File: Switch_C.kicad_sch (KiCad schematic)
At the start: 4 parts, among them U1601 TMCS1101A2UQDT

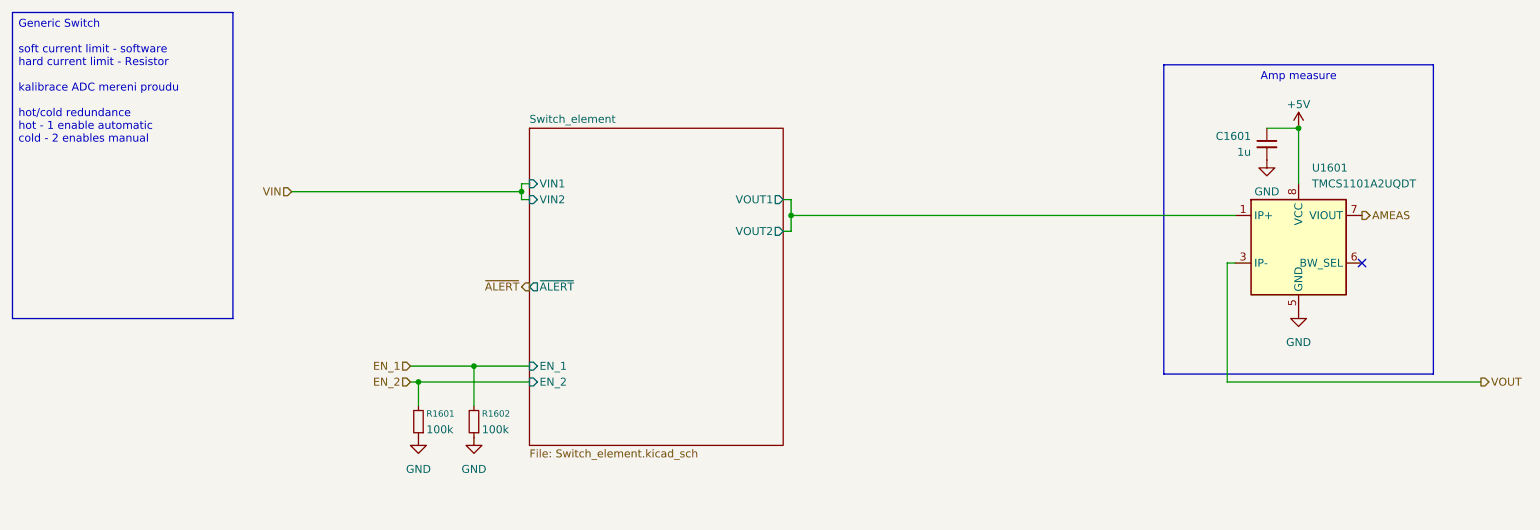
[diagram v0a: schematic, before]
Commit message: updated battery pack module; updated solar inputs module
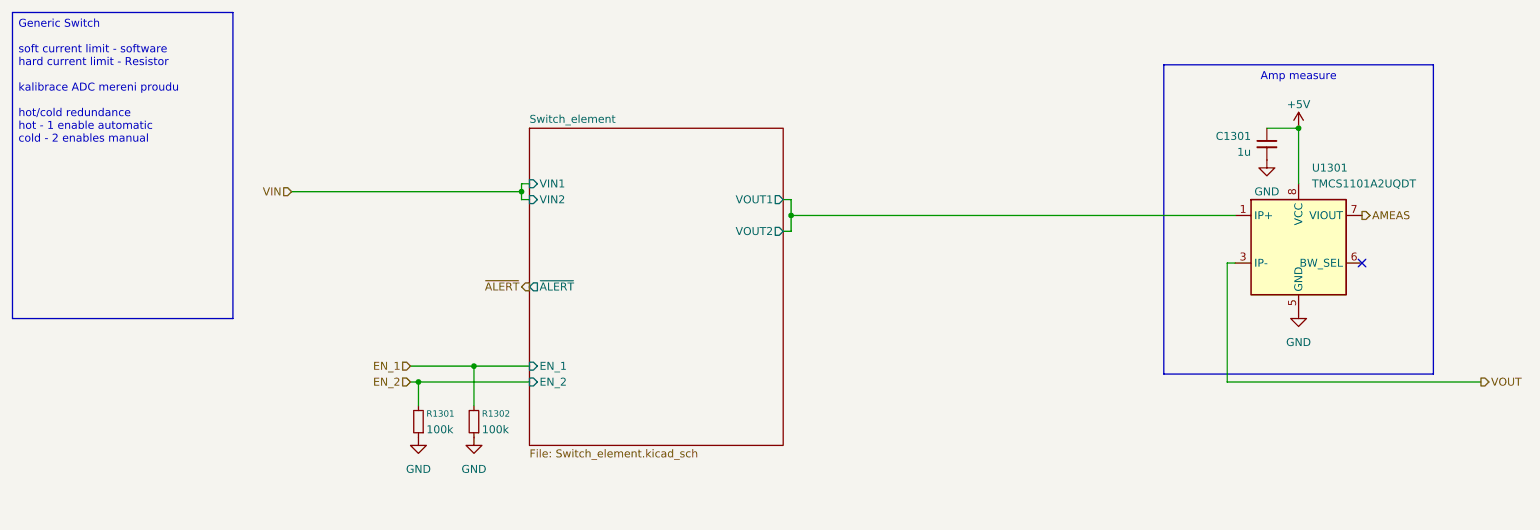
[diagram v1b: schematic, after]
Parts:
- renumbered C1601 to C1301, R1601 to R1301, R1602 to R1302, U1601 to U1301

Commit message: added values to most parts
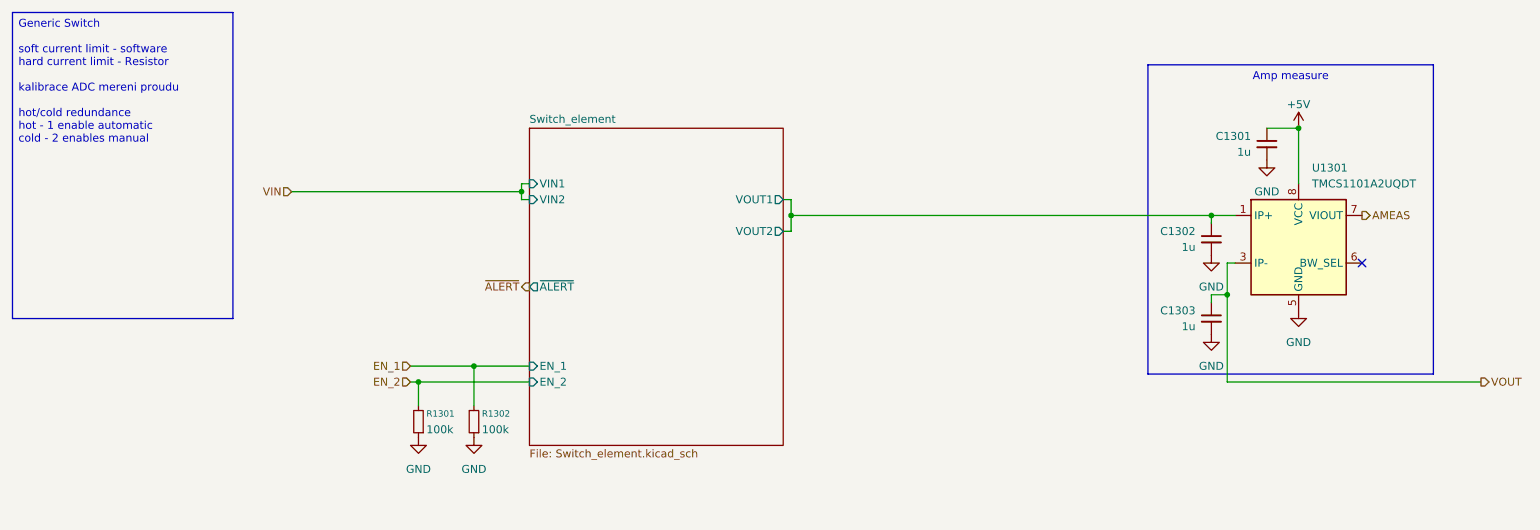
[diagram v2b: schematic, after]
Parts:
- added C1302, C1303: 1u, Capacitor_SMD:C_0603_1608Metric_Pad1.08x0.95mm_HandSolder, symbol Device:C_Small
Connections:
- net GND: now also C1302.2, C1303.2
- net Switch_element/VOUT1: now also C1302.1
- net VOUT: now also C1303.1

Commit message: deleted unused sheets, added standalone current measure sheet
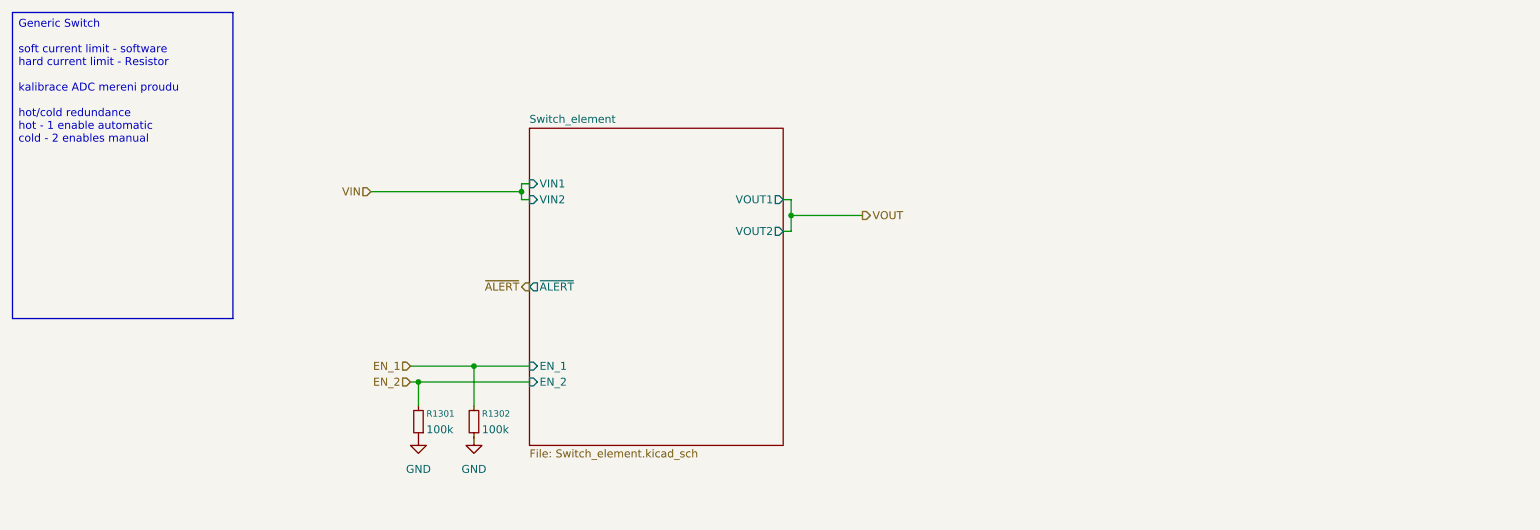
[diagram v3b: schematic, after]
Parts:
- removed C1301, C1302, C1303: 1u, Capacitor_SMD:C_0603_1608Metric_Pad1.08x0.95mm_HandSolder, symbol Device:C_Small
- removed U1301: TMCS1101A2UQDT, Package_SO:SOIC-8_3.9x4.9mm_P1.27mm, symbol Sensor_Current:ACS723xLCTR-40AB
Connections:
- no-connect marks 1 -> 0

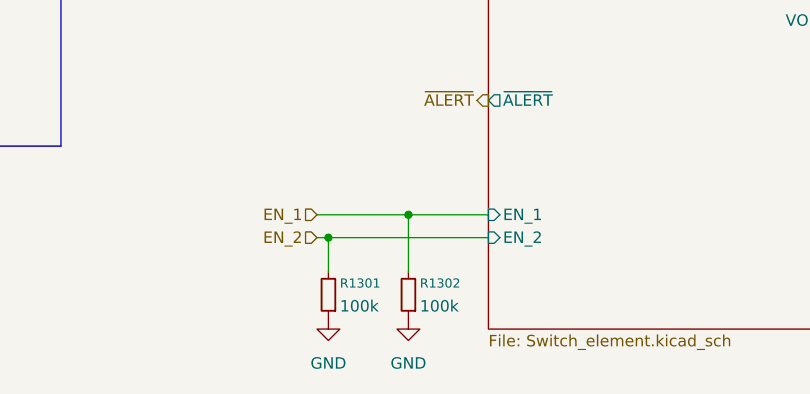
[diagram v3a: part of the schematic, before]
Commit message: wired channel alerts; added schematic for test pbc
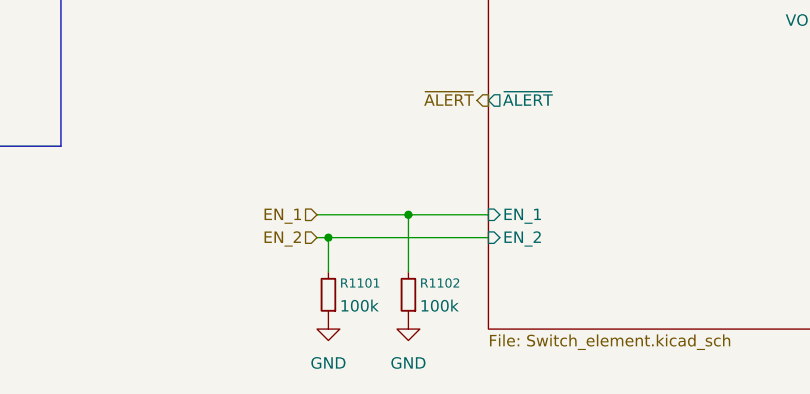
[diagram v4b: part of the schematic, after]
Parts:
- renumbered R1301 to R1101, R1302 to R1102
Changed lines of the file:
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@@
 		(on_board yes)
 		(dnp no)
-		(property "Reference" "R1301"
+		(property "Reference" "R1101"
 			(at 96.52 115.57 0)
 			(effects
@@
 		)
 		(instances
+			(project "TEST_PCB"
+				(path "/29496ace-b476-4f24-a65f-9da1dd70122c/877eed00-5750-4f47-bd20-90566d489da0"
+					(reference "R1101")
+					(unit 1)
+				)
+			)
 			(project "EPS"
 				(path "/94201994-47b8-4213-8d1a-05da12b2a7b0/8920358c-844b-40af-9382-a9a47367f2f9/18317d81-3057-4f2d-8dd0-207e3d519bfa"
@@
 		(on_board yes)
 		(dnp no)
-		(property "Reference" "R1302"
+		(property "Reference" "R1102"
 			(at 105.41 115.57 0)
 			(effects
@@
 		)
 		(instances
+			(project "TEST_PCB"
+				(path "/29496ace-b476-4f24-a65f-9da1dd70122c/877eed00-5750-4f47-bd20-90566d489da0"
+					(reference "R1102")
+					(unit 1)
+				)
+			)
 			(project "EPS"
 				(path "/94201994-47b8-4213-8d1a-05da12b2a7b0/8920358c-844b-40af-9382-a9a47367f2f9/18317d81-3057-4f2d-8dd0-207e3d519bfa"
@@
 		(dnp no)
 		(fields_autoplaced yes)
-		(property "Reference" "#PWR01301"
+		(property "Reference" "#PWR01101"
 			(at 95.25 125.73 0)
 			(effects
@@
 		)
 		(instances
+			(project "TEST_PCB"
+				(path "/29496ace-b476-4f24-a65f-9da1dd70122c/877eed00-5750-4f47-bd20-90566d489da0"
+					(reference "#PWR01101")
+					(unit 1)
+				)
+			)
 			(project "EPS"
 				(path "/94201994-47b8-4213-8d1a-05da12b2a7b0/8920358c-844b-40af-9382-a9a47367f2f9/18317d81-3057-4f2d-8dd0-207e3d519bfa"
@@
 		(dnp no)
 		(fields_autoplaced yes)
-		(property "Reference" "#PWR01302"
+		(property "Reference" "#PWR01102"
 			(at 104.14 125.73 0)
 			(effects
@@
 		)
 		(instances
+			(project "TEST_PCB"
+				(path "/29496ace-b476-4f24-a65f-9da1dd70122c/877eed00-5750-4f47-bd20-90566d489da0"
+					(reference "#PWR01102")
+					(unit 1)
+				)
+			)
 			(project "EPS"
 				(path "/94201994-47b8-4213-8d1a-05da12b2a7b0/8920358c-844b-40af-9382-a9a47367f2f9/18317d81-3057-4f2d-8dd0-207e3d519bfa"
@@
 				)
 			)
+			(project ""
+				(path "/877eed00-5750-4f47-bd20-90566d489da0"
+					(page "#")
+				)
+			)
+			(project "TEST_PCB"
+				(path "/29496ace-b476-4f24-a65f-9da1dd70122c/877eed00-5750-4f47-bd20-90566d489da0"
+					(page "18")
+				)
+			)

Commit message: reduced number of DCDC converter for PV panels; updated test pcb
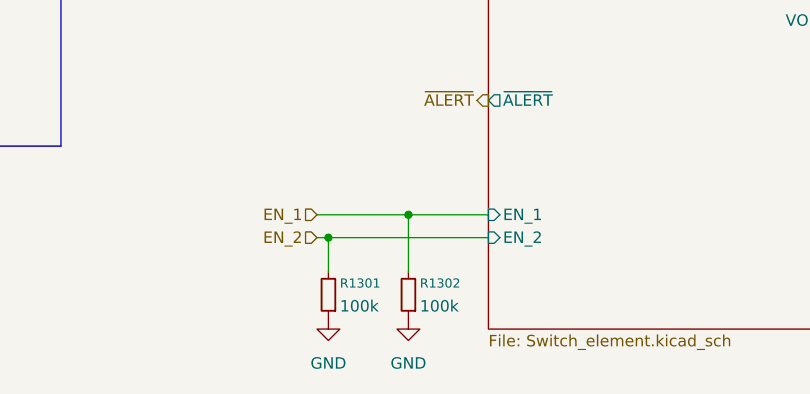
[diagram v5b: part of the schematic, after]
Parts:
- renumbered R1101 to R1301, R1102 to R1302

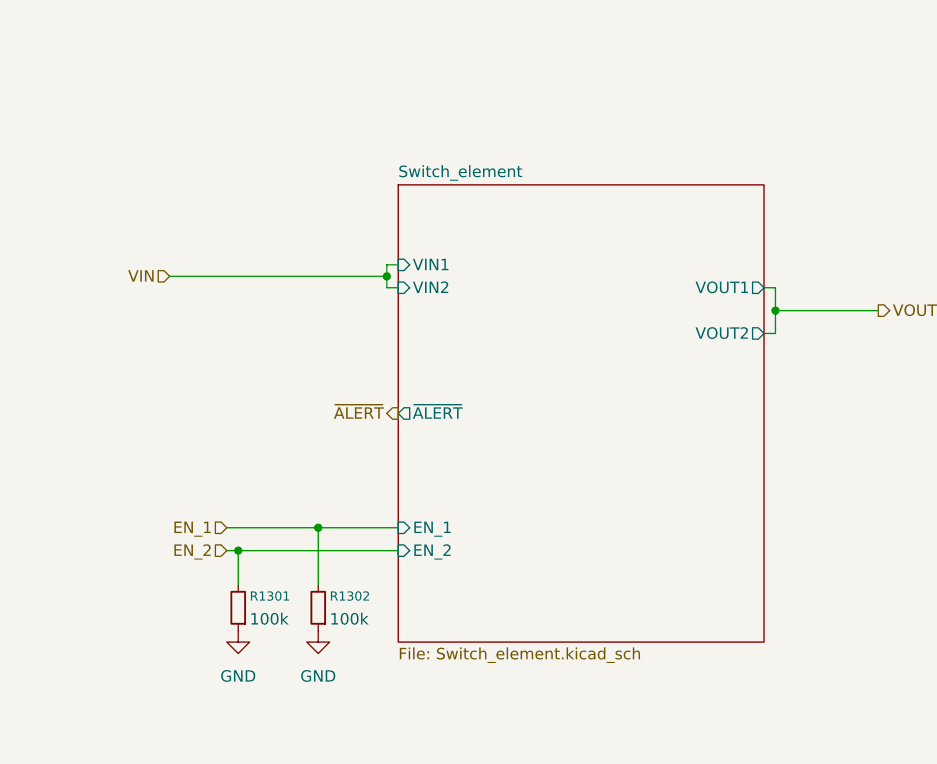
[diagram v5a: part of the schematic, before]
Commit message: restructurization of the entire project improved
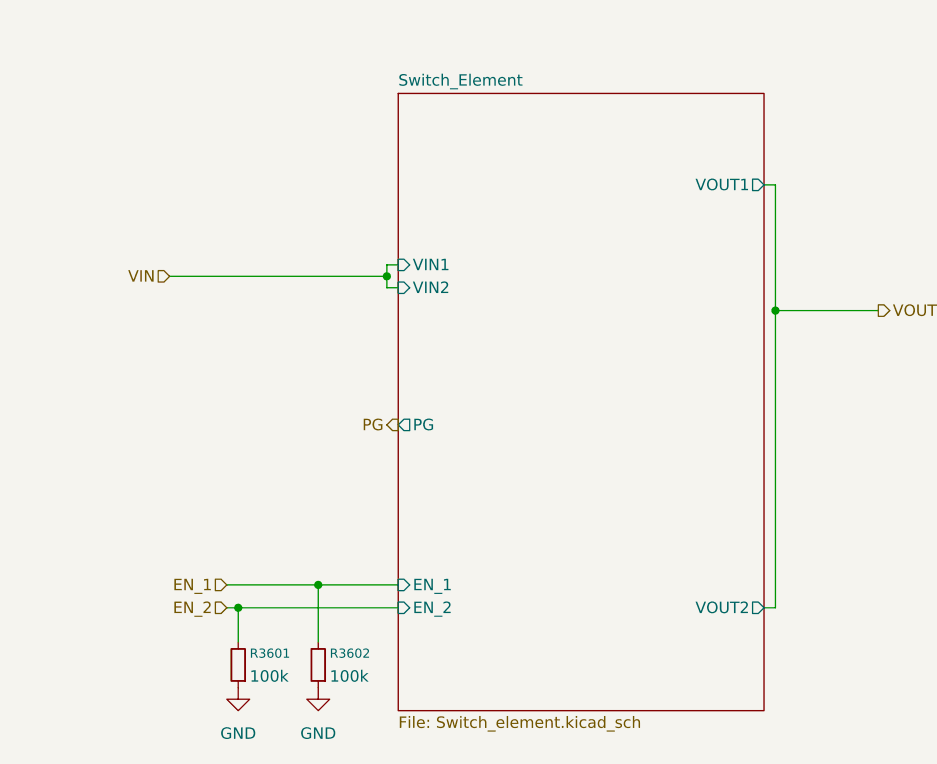
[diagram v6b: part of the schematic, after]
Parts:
- renumbered R1301 to R3601, R1302 to R3602
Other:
- removed sheet Switch_element
- added sheet Switch_Element (Switch_element.kicad_sch)
- moved on the sheet: R3601, R3602

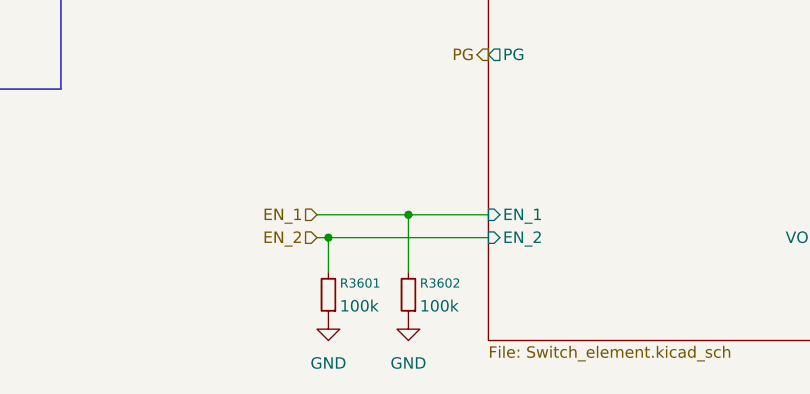
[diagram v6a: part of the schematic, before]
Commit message: added universal switch, added simples current source, reworked test schematic and pcb
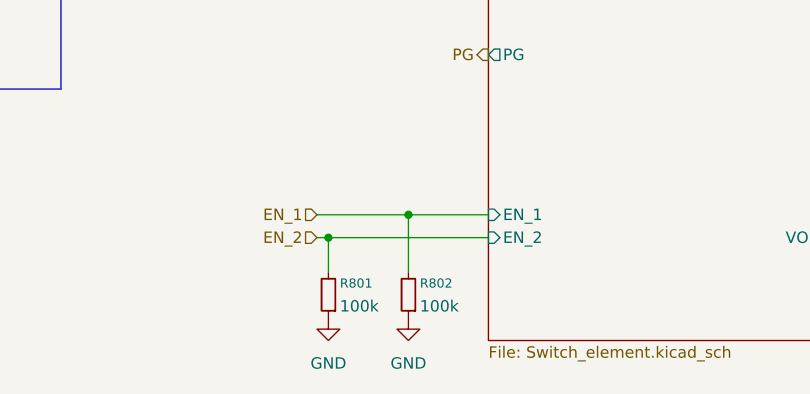
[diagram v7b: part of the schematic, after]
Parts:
- renumbered R3601 to R801, R3602 to R802
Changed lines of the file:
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@@
 		(on_board yes)
 		(dnp no)
-		(property "Reference" "R3601"
+		(property "Reference" "R801"
 			(at 96.52 121.92 0)
 			(effects
@@
 		)
 		(instances
+			(project "TEST_PCB"
+				(path "/29496ace-b476-4f24-a65f-9da1dd70122c/ece1b1ed-8c15-47cc-bd7f-cf79811fa9b5"
+					(reference "R801")
+					(unit 1)
+				)
+			)
 			(project "EPS_CORE"
 				(path "/43e5e7c8-e7e0-4528-9a3e-b1557849918d/170b50a7-486d-470b-9824-bd866624d07a"
@@
 		(on_board yes)
 		(dnp no)
-		(property "Reference" "R3602"
+		(property "Reference" "R802"
 			(at 105.41 121.92 0)
 			(effects
@@
 		)
 		(instances
+			(project "TEST_PCB"
+				(path "/29496ace-b476-4f24-a65f-9da1dd70122c/ece1b1ed-8c15-47cc-bd7f-cf79811fa9b5"
+					(reference "R802")
+					(unit 1)
+				)
+			)
 			(project "EPS_CORE"
 				(path "/43e5e7c8-e7e0-4528-9a3e-b1557849918d/170b50a7-486d-470b-9824-bd866624d07a"
@@
 		(dnp no)
 		(fields_autoplaced yes)
-		(property "Reference" "#PWR03601"
+		(property "Reference" "#PWR0165"
 			(at 95.25 132.08 0)
 			(effects
@@
 		)
 		(instances
+			(project "TEST_PCB"
+				(path "/29496ace-b476-4f24-a65f-9da1dd70122c/ece1b1ed-8c15-47cc-bd7f-cf79811fa9b5"
+					(reference "#PWR0165")
+					(unit 1)
+				)
+			)
 			(project "EPS_CORE"
 				(path "/43e5e7c8-e7e0-4528-9a3e-b1557849918d/170b50a7-486d-470b-9824-bd866624d07a"
@@
 		(dnp no)
 		(fields_autoplaced yes)
-		(property "Reference" "#PWR03602"
+		(property "Reference" "#PWR0166"
 			(at 104.14 132.08 0)
 			(effects
@@
 		)
 		(instances
+			(project "TEST_PCB"
+				(path "/29496ace-b476-4f24-a65f-9da1dd70122c/ece1b1ed-8c15-47cc-bd7f-cf79811fa9b5"
+					(reference "#PWR0166")
+					(unit 1)
+				)
+			)
 			(project "EPS_CORE"
 				(path "/43e5e7c8-e7e0-4528-9a3e-b1557849918d/170b50a7-486d-470b-9824-bd866624d07a"
@@
 				)
 			)
+			(project ""
+				(path "/41997ee6-fe7d-4257-91cc-69e8fbc1fd10"
+					(page "#")
+				)
+			)
